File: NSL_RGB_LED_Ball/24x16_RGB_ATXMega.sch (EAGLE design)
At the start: 120 parts, among them CON2 EXT, CON6 J8, CON8 J3, IC1 MEGA8-AI, IC2 TLC5947XLP, IC3 TLC5947XLP, IC4 TLC5947XLP, IC5 MCP73123, IC6 BLUETOOTH-RN41", IC7 MMA7455L, IC8 OPA344, Q1 BSH201, X1 16Mhz, X2 NX3225GA

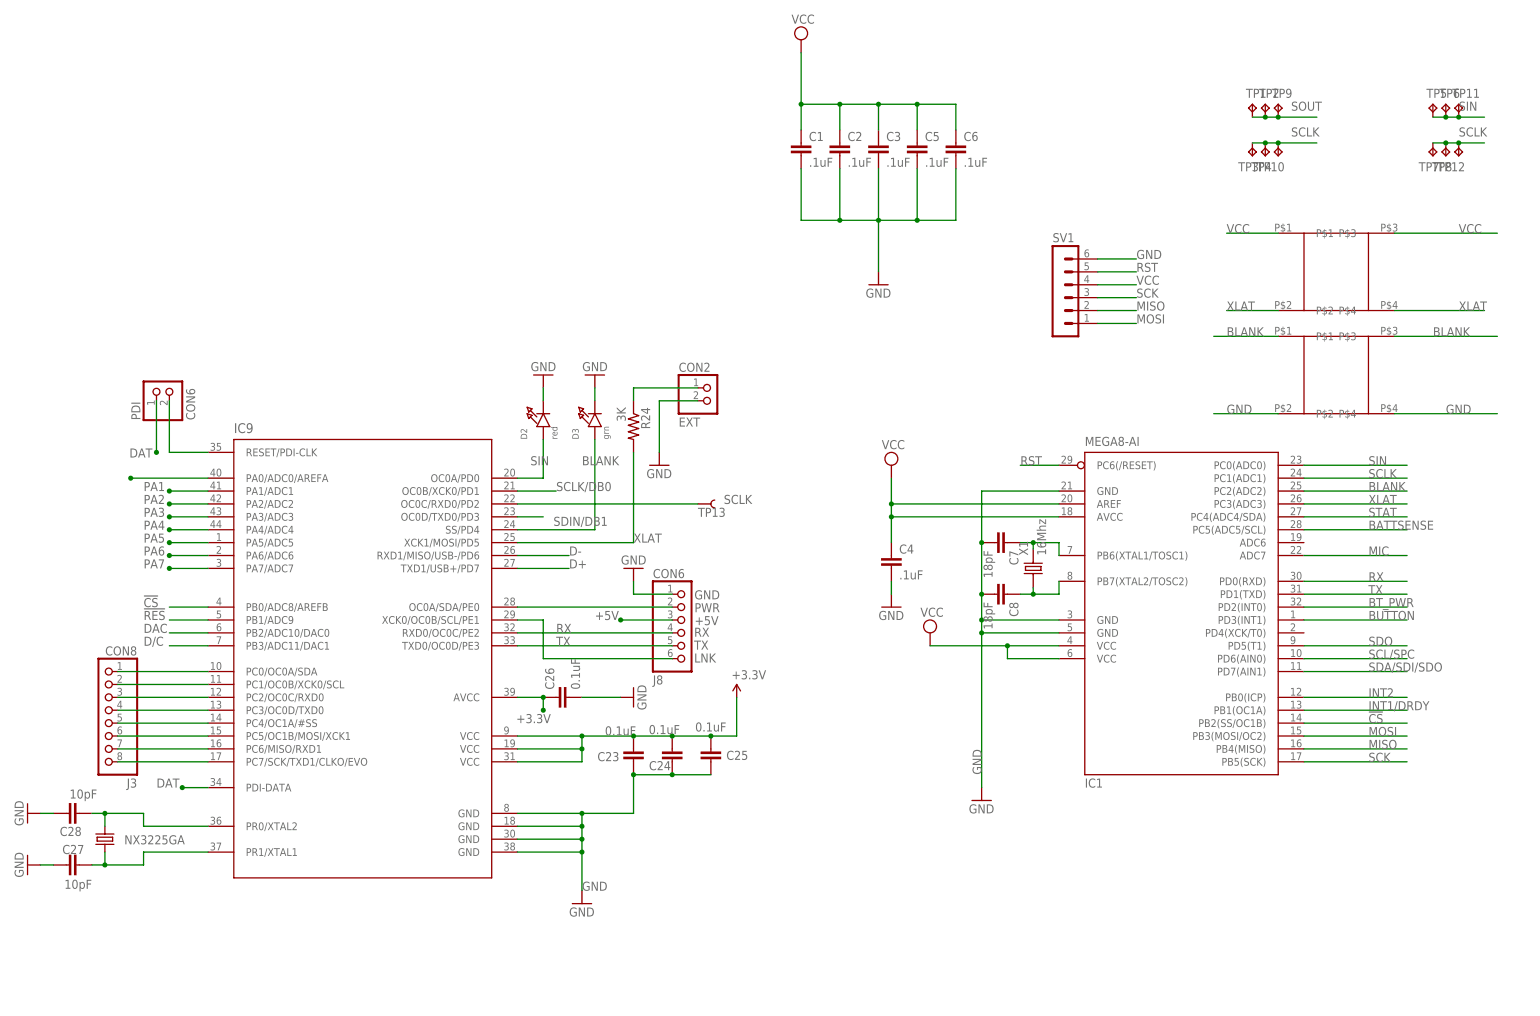
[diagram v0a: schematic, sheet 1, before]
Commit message: 
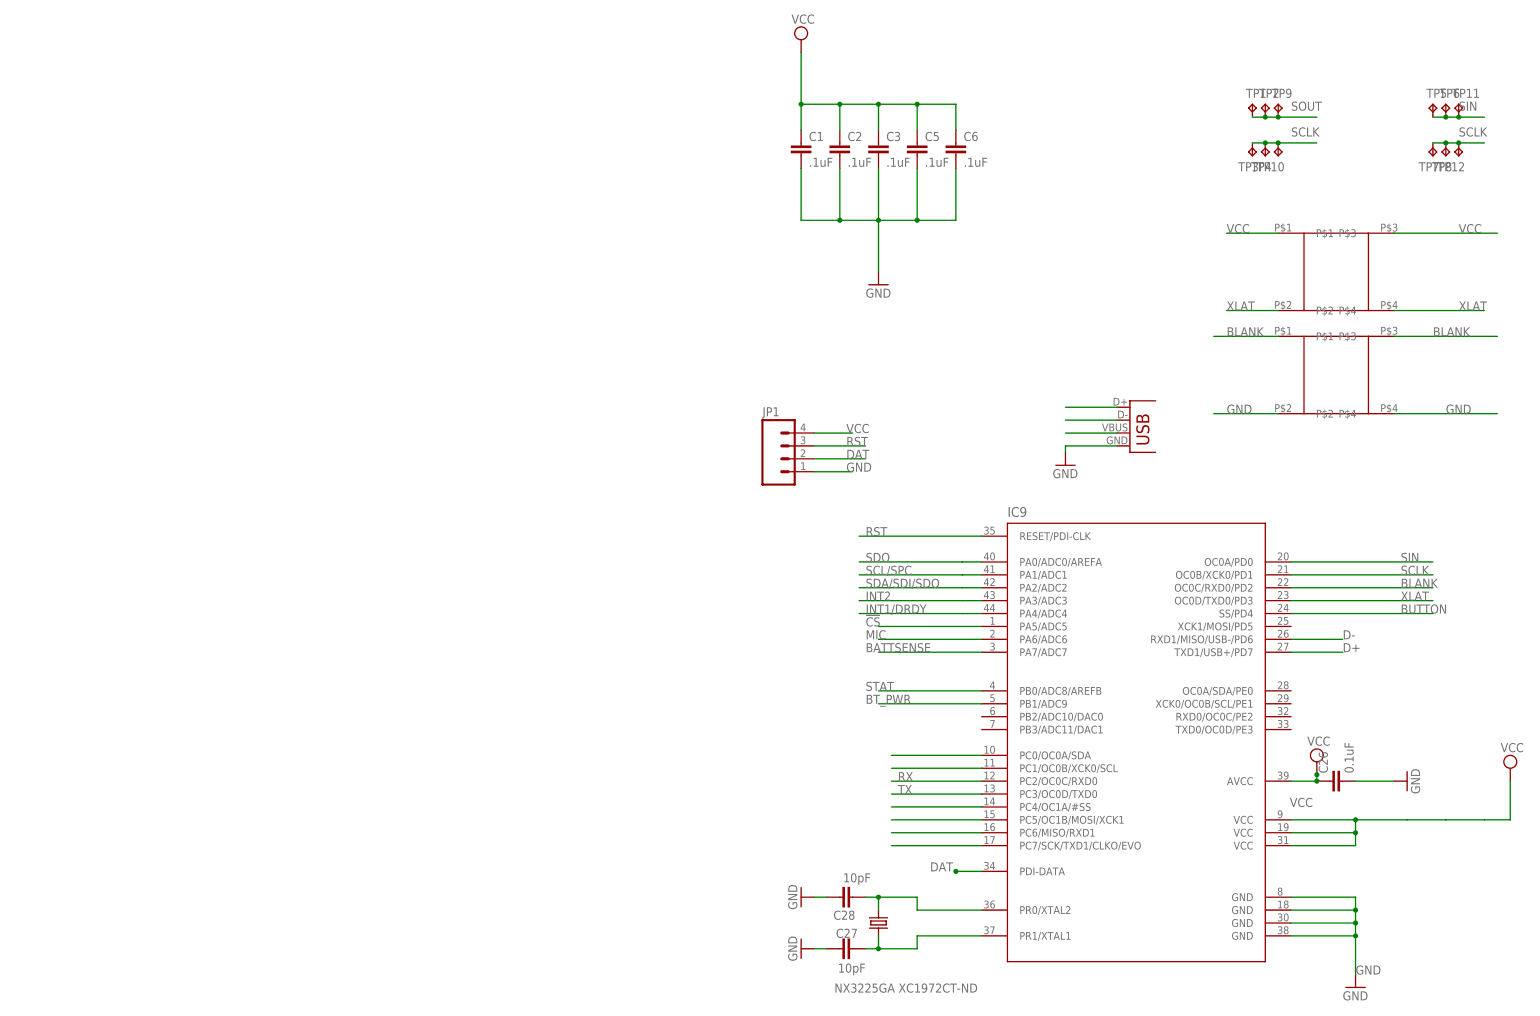
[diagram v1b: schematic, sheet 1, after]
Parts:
- removed C23, C24, C25: 0.1uF, SparkFun:CAP0805
- removed C4: .1uF, slice_noshift:CAP0805
- removed C7, C8: 18pF, slice_noshift:CAP0805
- removed CON2: EXT, microbuilder:HEADER-1X2
- removed CON6: J8, microbuilder:HEADER-1X6
- removed CON8: J3, microbuilder:HEADER-1X8
- removed D2: red, microbuilder:LED0805
- removed D3: grn, microbuilder:LED0805
- removed IC1: MEGA8-AI, atmel:MEGA8-AI
- removed PDI: CON6, microbuilder:HEADER-1X2
- removed R24: 3K, resistor:R-US_R0805
- removed SV1: (no value), NSL:MA06-1
- removed TP13: TEST-POINT2, SparkFun:TEST-POINT2
- removed X1: 16Mhz, NSL_MiniQuad:CRYSTAL-5032
- added JP1: (no value), SparkFun-Connectors:M04PTH
- added JP2: USBSMD, SparkFun-Connectors:USBSMD
- X2: value NX3225GA -> NX3225GA XC1972CT-ND
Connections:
- removed net !RES: IC9.PB1/ADC9
- removed net +2.048V: IC9.PA0/ADC0/AREFA
- removed net +3.3V: C23.2, C24.2, C25.2, C26.1, IC9.AVCC, IC9.VCC@1, IC9.VCC@2, IC9.VCC@3
- removed net +5V: CON6.3
- removed net D/C: IC9.PB3/ADC11/DAC1
- removed net DAC: IC9.PB2/ADC10/DAC0
- removed net LNK: CON6.6, IC9.XCK0/OC0B/SCL/PE1
- removed net MISO: IC1.PB4(MISO), SV1.2
- removed net MOSI: IC1.PB3(MOSI/OC2), SV1.1
- removed net N$26: CON8.3, IC9.PC2/OC0C/RXD0
- removed net N$27: CON8.4, IC9.PC3/OC0D/TXD0
- removed net N$31: CON2.1, R24.1
- removed net N$38: IC9.RESET/PDI-CLK, PDI.2
- removed net N$7: C7.1, IC1.PB6(XTAL1/TOSC1), X1.2
- removed net N$8: C8.1, IC1.PB7(XTAL2/TOSC2), X1.1
- removed net PA1: IC9.PA1/ADC1
- removed net PA2: IC9.PA2/ADC2
- removed net PA3: IC9.PA3/ADC3
- removed net PA4: IC9.PA4/ADC4
- removed net PA5: IC9.PA5/ADC5
- removed net PA6: IC9.PA6/ADC6
- removed net PA7: IC9.PA7/ADC7
- removed net PWR: CON6.2, IC9.OC0A/SDA/PE0
- removed net SCK: IC1.PB5(SCK), SV1.3
- removed net SCLK/DB0: IC9.OC0B/XCK0/PD1
- removed net SDIN/DB1: IC9.OC0D/TXD0/PD3
- net !CS: now also IC9.PA5/ADC5; no longer IC1.PB2(SS/OC1B), IC9.PB0/ADC8/AREFB
- net BATTSENSE: now also IC9.PA7/ADC7; no longer IC1.PC5(ADC5/SCL)
- net BLANK: now also IC9.OC0C/RXD0/PD2; no longer D3.A, IC1.PC2(ADC2), IC9.SS/PD4
- net BT_PWR: now also IC9.PB1/ADC9; no longer IC1.PD2(INT0)
- net BUTTON: now also IC9.SS/PD4; no longer IC1.PD3(INT1)
- net CHARGE: now also JP2.VBUS
- net D+: now also JP2.D+
- net D-: now also JP2.D-
- net DAT: now also JP1.2; no longer PDI.1
- net GND: now also JP1.1, JP2.GND; no longer C23.1, C24.1, C25.1, C4.2, C7.2, C8.2, CON2.2, CON6.1, D2.C, D3.C, IC1.GND, IC1.GND@1, IC1.GND@2, SV1.6
- net INT1/DRDY: now also IC9.PA4/ADC4; no longer IC1.PB1(OC1A)
- net INT2: now also IC9.PA3/ADC3; no longer IC1.PB0(ICP)
- net J3: no longer CON8.5
- net MIC: now also IC9.PA6/ADC6; no longer IC1.ADC7
- net N$22: no longer CON8.1
- net N$25: no longer CON8.2
- net N$28: no longer CON8.6
- net N$29: no longer CON8.7
- net N$30: no longer CON8.8
- net RST: now also IC9.RESET/PDI-CLK, JP1.3; no longer IC1.PC6(/RESET), SV1.5
- net RX: now also IC9.PC2/OC0C/RXD0; no longer CON6.4, IC1.PD0(RXD), IC9.RXD0/OC0C/PE2
- net SCL/SPC: now also IC9.PA1/ADC1; no longer IC1.PD6(AIN0)
- net SCLK: now also IC9.OC0B/XCK0/PD1; no longer IC1.PC1(ADC1), IC9.OC0C/RXD0/PD2, TP13.1
- net SDA/SDI/SDO: now also IC9.PA2/ADC2; no longer IC1.PD7(AIN1)
- net SDO: now also IC9.PA0/ADC0/AREFA; no longer IC1.PD5(T1)
- net SIN: no longer D2.A, IC1.PC0(ADC0)
- net STAT: now also IC9.PB0/ADC8/AREFB; no longer IC1.PC4(ADC4/SDA)
- net TX: now also IC9.PC3/OC0D/TXD0; no longer CON6.5, IC1.PD1(TXD), IC9.TXD0/OC0D/PE3
- net VCC: now also C26.1, IC9.AVCC, IC9.VCC@1, IC9.VCC@2, IC9.VCC@3, JP1.4; no longer C4.1, IC1.AREF, IC1.AVCC, IC1.VCC@1, IC1.VCC@2, SV1.4
- net XLAT: now also IC9.OC0D/TXD0/PD3; no longer IC1.PC3(ADC3), IC9.XCK1/MOSI/PD5, R24.2
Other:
- moved on the sheet: C26, C27, C28, IC9

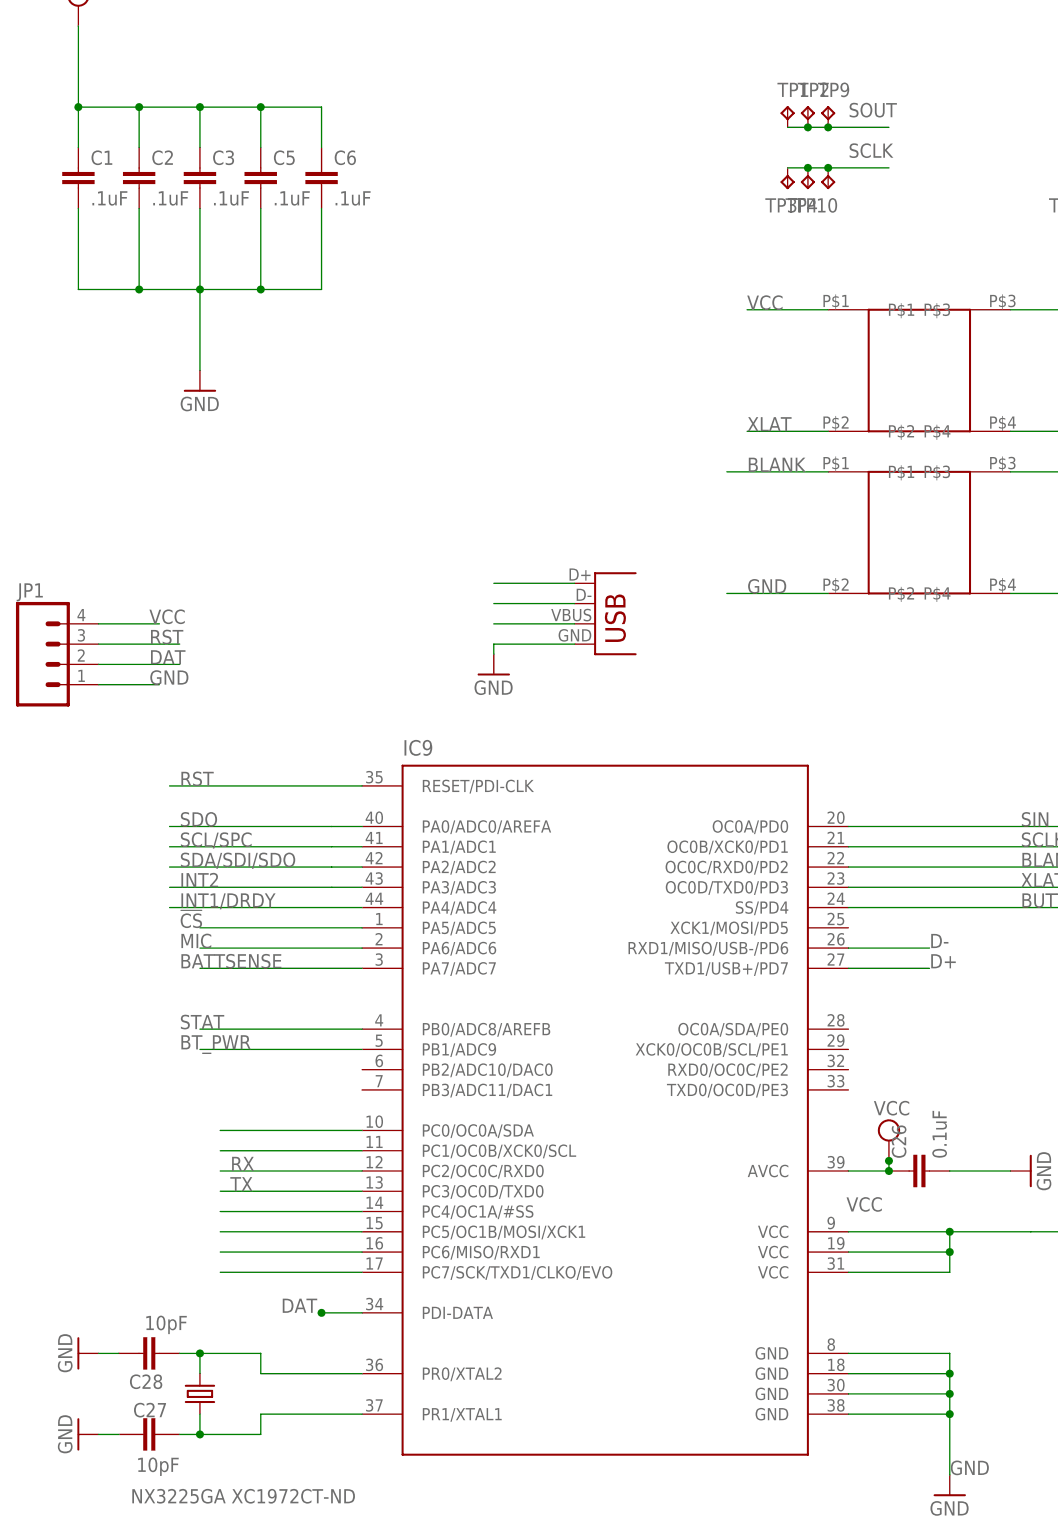
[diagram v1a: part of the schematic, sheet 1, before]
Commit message: 
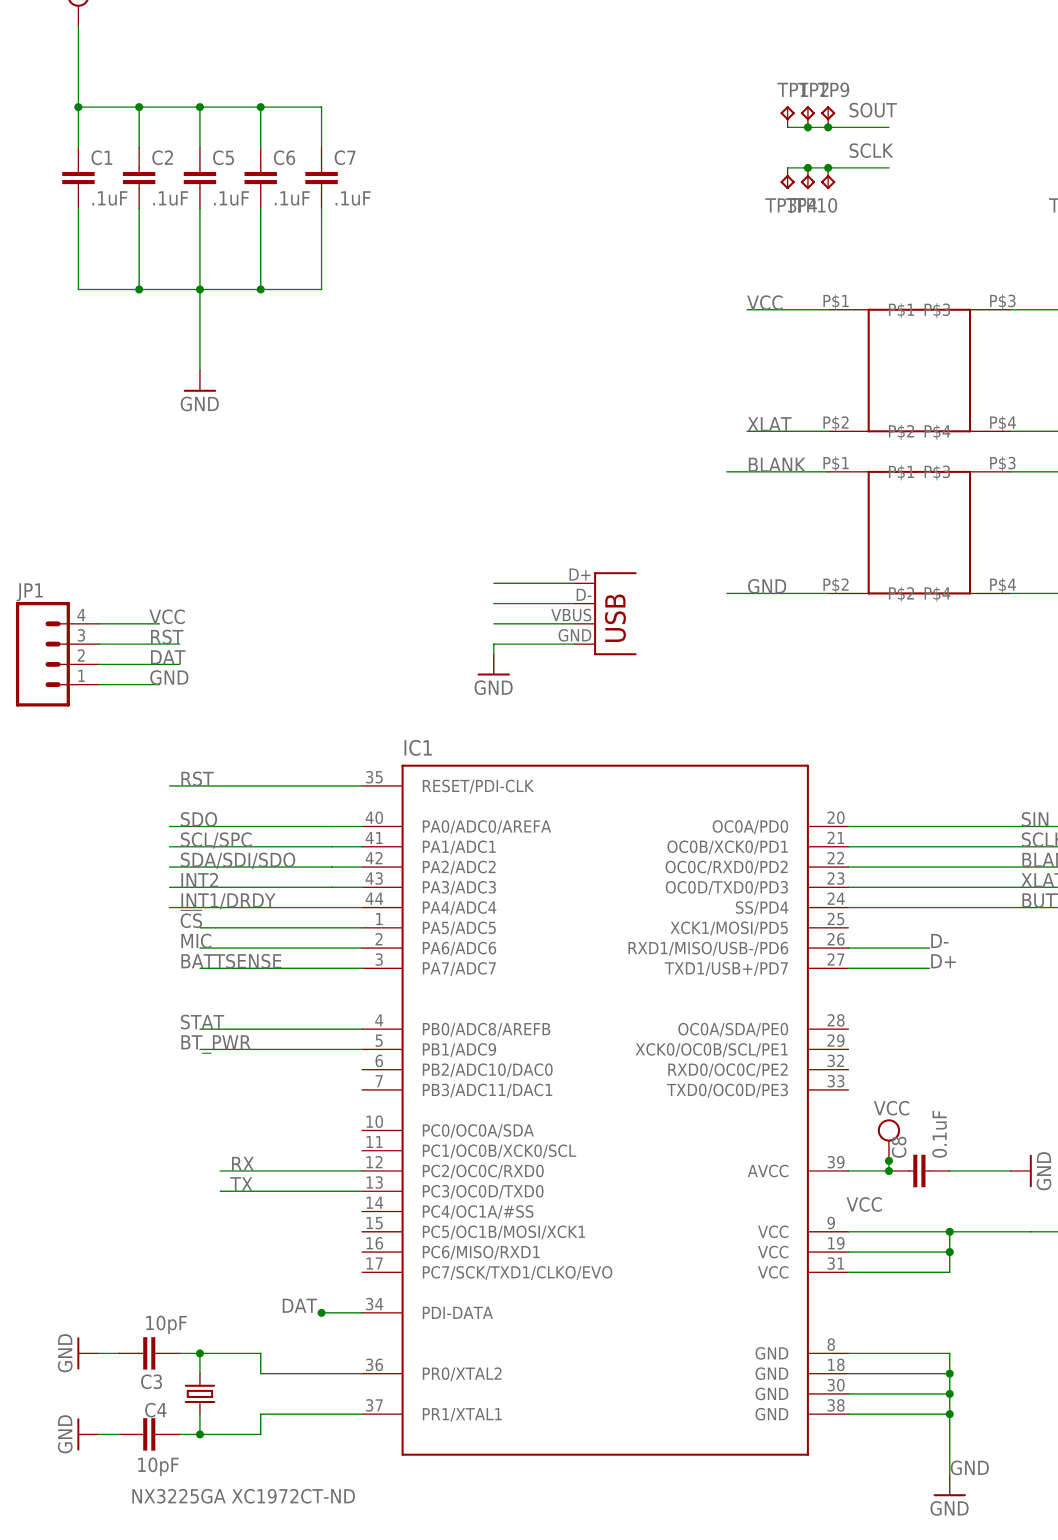
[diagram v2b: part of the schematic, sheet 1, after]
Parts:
- removed C28: 10pF, SparkFun:CAP0805
- added C7: .1uF, slice_noshift:CAP0805
- C15: value .1uF -> 1uF; device SparkFun:CAP0805 -> 24x16_RGB:CAP0805; MPN 08055C105MAT2A -> 08055D105KAT2A; OC_NEWARK 73T5385 -> 66M3779
- C16: value 0.1uF -> 1uF; device SparkFun:CAP0805 -> 24x16_RGB:CAP0805; MPN 08055C104K4T2A -> 08055D105KAT2A; OC_NEWARK 95W2729 -> 66M3779
- C17: value 4.7uF -> .1uF; MPN 08053D475KAT2A -> 08055C105MAT2A; OC_NEWARK 15P4053 -> 73T5385
- C18: value 1uF -> 0.1uF; MPN 08055D105KAT2A -> 08055C104K4T2A; OC_NEWARK 66M3779 -> 95W2729
- C19: value .1uF -> 4.7uF; MPN 08055C105MAT2A -> 08053D475KAT2A; OC_NEWARK 73T5385 -> 15P4053
- C20: value 12pF -> 1uF; MF AVX CORPORATION -> (none); MPN 08055A120JAT2A -> 08055D105KAT2A; OC_NEWARK 30H0781 -> 66M3779
- C21: value 1uF -> .1uF; device 24x16_RGB:CAP0805 -> SparkFun:CAP0805; MPN 08055D105KAT2A -> 08055C105MAT2A; OC_NEWARK 66M3779 -> 73T5385
- C22: value 1uF -> 12pF; device 24x16_RGB:CAP0805 -> SparkFun:CAP0805; MF (none) -> AVX CORPORATION; MPN 08055D105KAT2A -> 08055A120JAT2A; OC_NEWARK 66M3779 -> 30H0781
- C3: value .1uF -> 10pF; device slice_noshift:CAP0805 -> SparkFun:CAP0805; MPN 08055C105MAT2A -> (none); OC_NEWARK 73T5385 -> (none)
- renumbered C26 to C8, C27 to C4, IC9 to IC1, X2 to X1
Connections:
- removed net J3: IC1.PC4/OC1A/#SS
- removed net N$22: IC1.PC0/OC0A/SDA
- removed net N$25: IC1.PC1/OC0B/XCK0/SCL
- removed net N$28: IC1.PC5/OC1B/MOSI/XCK1
- removed net N$29: IC1.PC6/MISO/RXD1
- removed net N$30: IC1.PC7/SCK/TXD1/CLKO/EVO
- net GND: now also C16.2, C17.2, C20.1, C3.1, C7.2; no longer C16.1, C19.2, C22.2, C28.1, C3.2
- net MIC: now also C22.1; no longer C20.1
- net N$14: now also C19.2; no longer C17.2
- net N$15: now also C19.1; no longer C17.1
- net N$16: now also C20.2; no longer C18.2
- net N$17: now also C21.1, C22.2; no longer C19.1, C20.2
- net N$36: now also C3.2; no longer C28.2
- net VCC: now also C15.1, C16.1, C18.2, C7.1; no longer C16.2, C21.1, C22.1, C3.1
- net VDD: now also C17.1; no longer C15.1
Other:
- moved on the sheet: C19, C20, C3, C5, C6

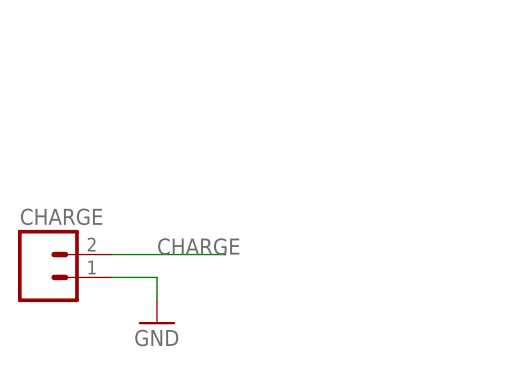
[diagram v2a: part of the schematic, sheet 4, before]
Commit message: 
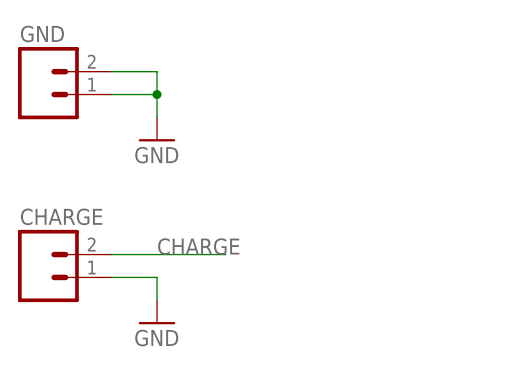
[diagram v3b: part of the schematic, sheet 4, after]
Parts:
- added GND: (no value), SparkFun:M02PTH
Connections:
- net GND: now also GND.1, GND.2
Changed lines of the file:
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@@
 <part name="JP2" library="SparkFun-Connectors" deviceset="USB" device="SMD"/>
 <part name="GND12" library="SparkFun" deviceset="GND" device=""/>
+<part name="GND" library="SparkFun" deviceset="M02" device="PTH">
+<attribute name="MF" value=""/>
+<attribute name="MPN" value=""/>
+<attribute name="OC_NEWARK" value="unknown"/>
+</part>
+<part name="GND13" library="SparkFun" deviceset="GND" device=""/>
 </parts>
 <sheets>
@@
 <attribute name="MPN" x="114.3" y="-7.62" size="1.778" layer="96" display="off"/>
 </instance>
+<instance part="GND" gate="G$1" x="-50.8" y="48.26">
+<attribute name="OC_NEWARK" x="-50.8" y="48.26" size="1.778" layer="96" display="off"/>
+<attribute name="MF" x="-50.8" y="48.26" size="1.778" layer="96" display="off"/>
+<attribute name="MPN" x="-50.8" y="48.26" size="1.778" layer="96" display="off"/>
+</instance>
+<instance part="GND13" gate="1" x="-38.1" y="43.18"/>
 </instances>
 <busses>
@@
 <pinref part="GND16" gate="1" pin="GND"/>
 </segment>
-</net>
+<segment>
+<pinref part="GND" gate="G$1" pin="2"/>
+<pinref part="GND13" gate="1" pin="GND"/>
+<wire x1="-43.18" y1="50.8" x2="-38.1" y2="50.8" width="0.1524" layer="91"/>
+<wire x1="-38.1" y1="50.8" x2="-38.1" y2="48.26" width="0.1524" layer="91"/>
+<pinref part="GND" gate="G$1" pin="1"/>
+<wire x1="-38.1" y1="48.26" x2="-38.1" y2="45.72" width="0.1524" layer="91"/>
+<wire x1="-43.18" y1="48.26" x2="-38.1" y2="48.26" width="0.1524" layer="91"/>
+<junction x="-38.1" y="48.26"/>
+</segment>
+</net>

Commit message: 
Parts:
- added D1: SSB44-E3/52T, diode:DIODE-DO214AA
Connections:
- new net N$7: D1.A, JP2.VBUS
- net CHARGE: now also D1.C; no longer JP2.VBUS
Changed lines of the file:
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@@
 </part>
 <part name="GND13" library="SparkFun" deviceset="GND" device=""/>
+<part name="D1" library="diode" deviceset="DIODE-" device="DO214AA" value="SSB44-E3/52T"/>
 </parts>
 <sheets>
@@
 <instance part="JP2" gate="G$1" x="-8.89" y="6.35"/>
 <instance part="GND12" gate="1" x="-21.59" y="2.54"/>
+<instance part="D1" gate="G$1" x="-24.13" y="8.89" rot="R180"/>
 </instances>
 <busses>
@@
 <net name="CHARGE" class="0">
 <segment>
+<wire x1="-26.67" y1="8.89" x2="-44.45" y2="8.89" width="0.1524" layer="91"/>
+<pinref part="D1" gate="G$1" pin="C"/>
+<label x="-35.56" y="7.62" size="1.778" layer="95" rot="R180"/>
+</segment>
+</net>
+<net name="N$7" class="0">
+<segment>
+<pinref part="JP2" gate="G$1" pin="VBUS"/>
+<pinref part="D1" gate="G$1" pin="A"/>
 <wire x1="-11.43" y1="8.89" x2="-21.59" y2="8.89" width="0.1524" layer="91"/>
-<pinref part="JP2" gate="G$1" pin="VBUS"/>
-</segment>
-</net>
+</segment>
+</net>
